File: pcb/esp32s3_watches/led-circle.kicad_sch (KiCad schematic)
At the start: 60 parts

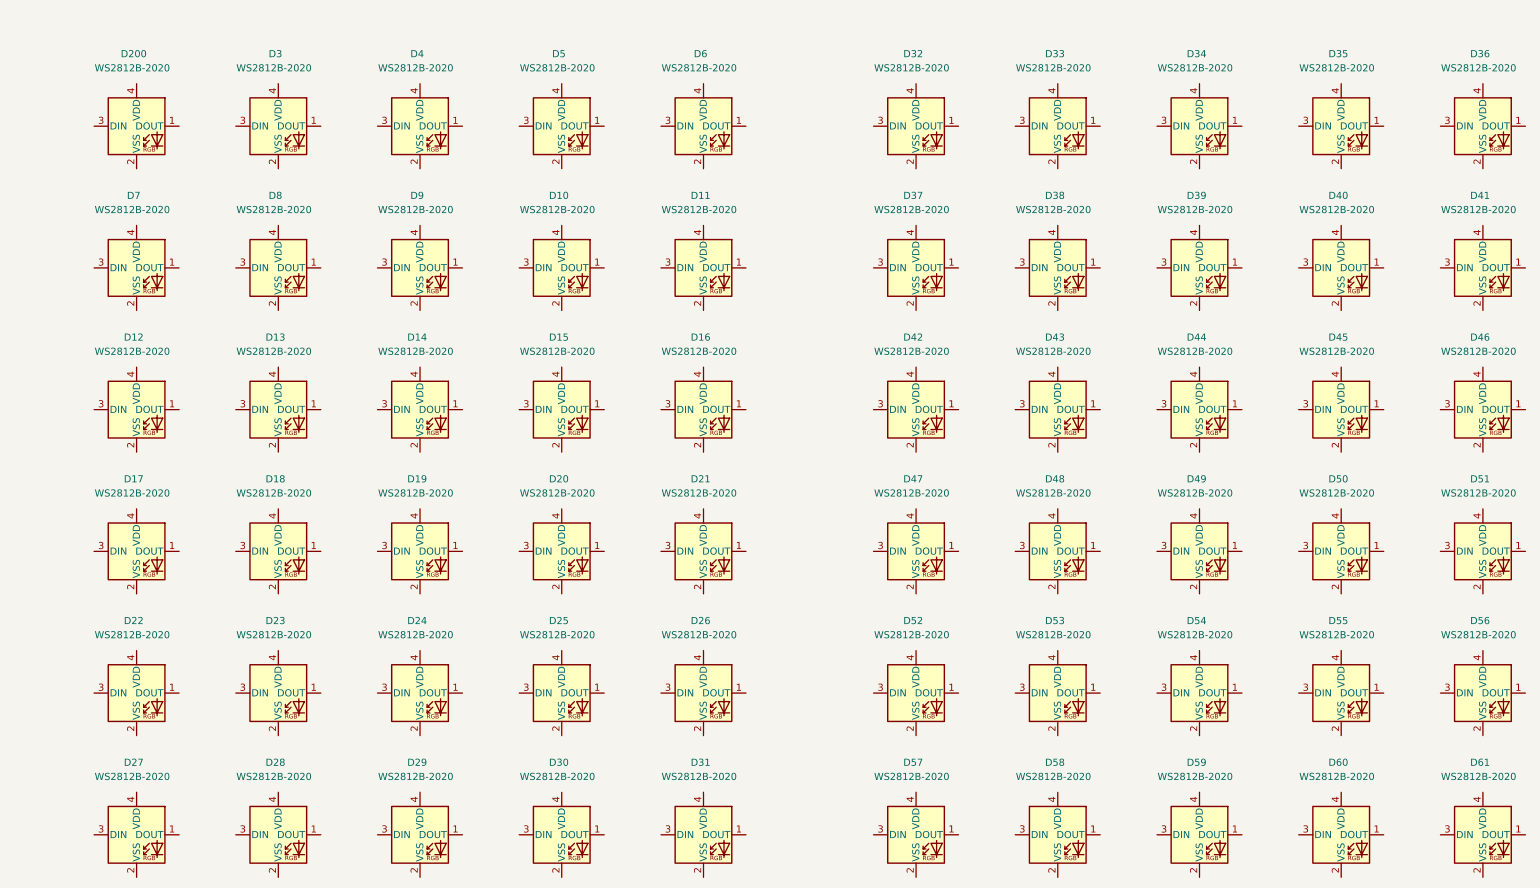
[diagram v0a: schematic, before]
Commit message: Update SD card connection
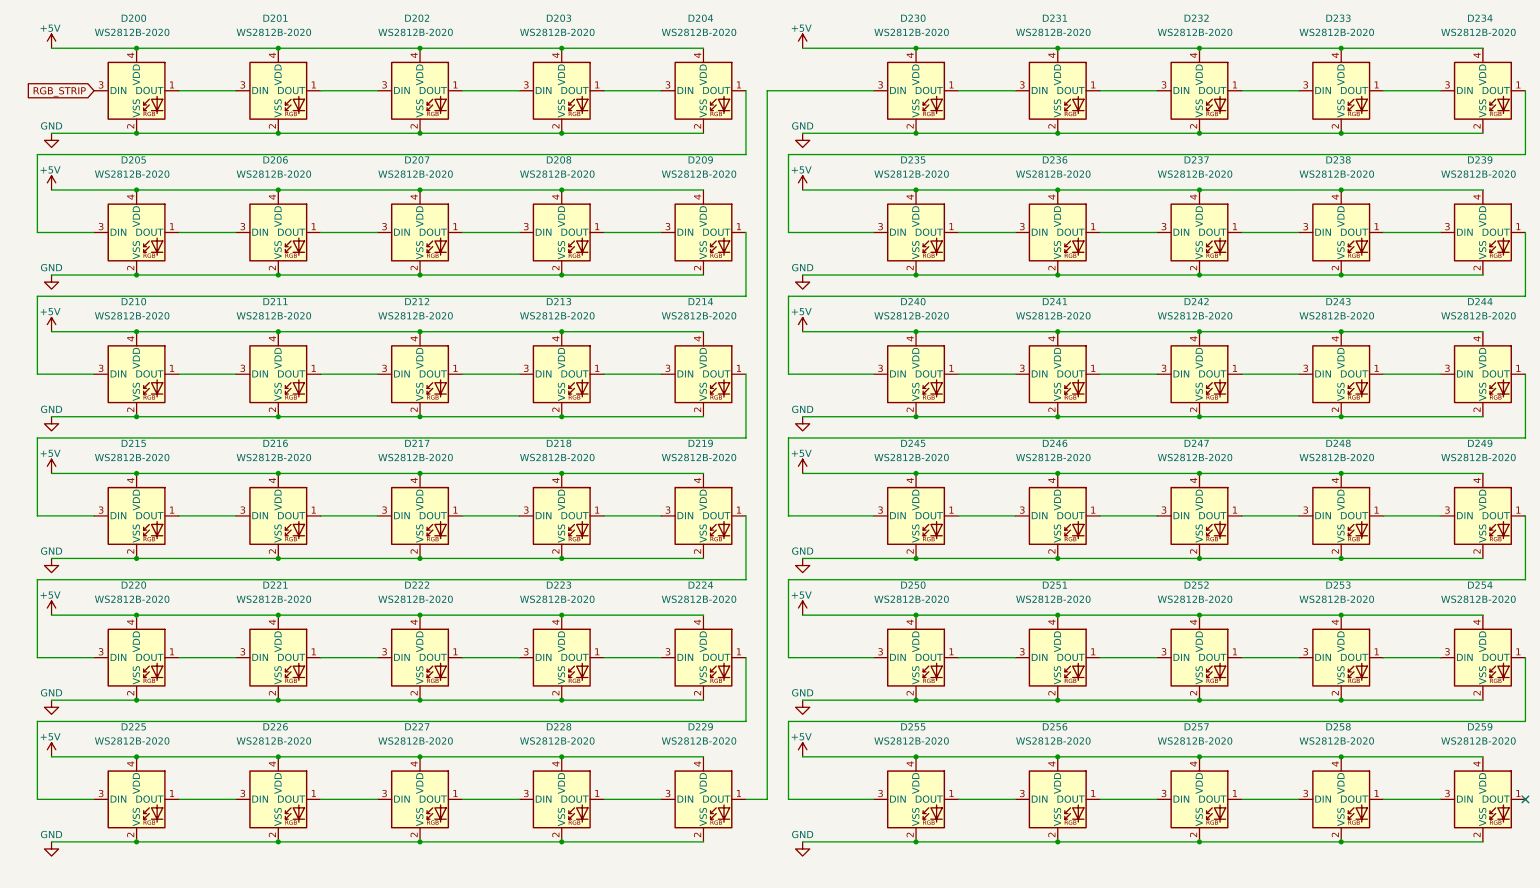
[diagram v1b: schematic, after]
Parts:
- renumbered D3 to D201, D4 to D202, D5 to D203, D6 to D204, D7 to D205, D8 to D206, D9 to D207, D10 to D208, D11 to D209, D12 to D210, D13 to D211, D14 to D212, D15 to D213, D16 to D214, D17 to D215, D18 to D216, D19 to D217, D20 to D218, D21 to D219, D22 to D220, D23 to D221, D24 to D222, D25 to D223, D26 to D224, D27 to D225, D28 to D226, D29 to D227, D30 to D228, D31 to D229, D32 to D230, D33 to D231, D34 to D232, D35 to D233, D36 to D234, D37 to D235, D38 to D236, D39 to D237, D40 to D238, D41 to D239, D42 to D240, D43 to D241, D44 to D242, D45 to D243, D46 to D244, D47 to D245, D48 to D246, D49 to D247, D50 to D248, D51 to D249, D52 to D250, D53 to D251, D54 to D252, D55 to D253, D56 to D254, D57 to D255, D58 to D256, D59 to D257, D60 to D258, D61 to D259
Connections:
- net at D256.1 (DOUT): now also D257.3 (DIN)
- net GND: now reaches D256.2 (VSS)
- net GND: now also D200.2 (VSS), D201.2 (VSS), D202.2 (VSS), D203.2 (VSS), D204.2 (VSS), D205.2 (VSS), D206.2 (VSS), D207.2 (VSS), D208.2 (VSS), D209.2 (VSS), D210.2 (VSS), D211.2 (VSS), D212.2 (VSS), D213.2 (VSS), D214.2 (VSS), D215.2 (VSS), D216.2 (VSS), D217.2 (VSS), D218.2 (VSS), D219.2 (VSS), D220.2 (VSS), D221.2 (VSS), D222.2 (VSS), D223.2 (VSS), D224.2 (VSS), D225.2 (VSS), D226.2 (VSS), D227.2 (VSS), D228.2 (VSS), D229.2 (VSS), D230.2 (VSS), D231.2 (VSS), D232.2 (VSS), D233.2 (VSS), D234.2 (VSS), D235.2 (VSS), D236.2 (VSS), D237.2 (VSS), D238.2 (VSS), D239.2 (VSS), D240.2 (VSS), D241.2 (VSS), D242.2 (VSS), D243.2 (VSS), D244.2 (VSS), D245.2 (VSS), D246.2 (VSS), D247.2 (VSS), D248.2 (VSS), D249.2 (VSS), D250.2 (VSS), D251.2 (VSS), D252.2 (VSS), D253.2 (VSS), D254.2 (VSS), D255.2 (VSS), D257.2 (VSS), D258.2 (VSS), D259.2 (VSS)
- net at D256.3 (DIN): now also D255.1 (DOUT)
- net +5V: now reaches D256.4 (VDD)
- net +5V: now also D200.4 (VDD), D201.4 (VDD), D202.4 (VDD), D203.4 (VDD), D204.4 (VDD), D205.4 (VDD), D206.4 (VDD), D207.4 (VDD), D208.4 (VDD), D209.4 (VDD), D210.4 (VDD), D211.4 (VDD), D212.4 (VDD), D213.4 (VDD), D214.4 (VDD), D215.4 (VDD), D216.4 (VDD), D217.4 (VDD), D218.4 (VDD), D219.4 (VDD), D220.4 (VDD), D221.4 (VDD), D222.4 (VDD), D223.4 (VDD), D224.4 (VDD), D225.4 (VDD), D226.4 (VDD), D227.4 (VDD), D228.4 (VDD), D229.4 (VDD), D230.4 (VDD), D231.4 (VDD), D232.4 (VDD), D233.4 (VDD), D234.4 (VDD), D235.4 (VDD), D236.4 (VDD), D237.4 (VDD), D238.4 (VDD), D239.4 (VDD), D240.4 (VDD), D241.4 (VDD), D242.4 (VDD), D243.4 (VDD), D244.4 (VDD), D245.4 (VDD), D246.4 (VDD), D247.4 (VDD), D248.4 (VDD), D249.4 (VDD), D250.4 (VDD), D251.4 (VDD), D252.4 (VDD), D253.4 (VDD), D254.4 (VDD), D255.4 (VDD), D257.4 (VDD), D258.4 (VDD), D259.4 (VDD)
- net at D246.1 (DOUT): now also D247.3 (DIN)
- net at D246.3 (DIN): now also D245.1 (DOUT)
- net at D215.1 (DOUT): now also D216.3 (DIN)
- net at D215.3 (DIN): now also D214.1 (DOUT)
- net at D200.1 (DOUT): now also D201.3 (DIN)
- net RGB_STRIP: now reaches D200.3 (DIN)
- net at D213.1 (DOUT): now also D214.3 (DIN)
- net at D213.3 (DIN): now also D212.1 (DOUT)
- net at D202.1 (DOUT): now also D203.3 (DIN)
- net at D202.3 (DIN): now also D201.1 (DOUT)
- net at D252.1 (DOUT): now also D253.3 (DIN)
- net at D252.3 (DIN): now also D251.1 (DOUT)
- net at D211.1 (DOUT): now also D212.3 (DIN)
- net at D211.3 (DIN): now also D210.1 (DOUT)
- net at D236.1 (DOUT): now also D237.3 (DIN)
- net at D236.3 (DIN): now also D235.1 (DOUT)
- net at D248.1 (DOUT): now also D249.3 (DIN)
- net at D248.3 (DIN): now also D247.1 (DOUT)
- net at D224.1 (DOUT): now also D225.3 (DIN)
- net at D224.3 (DIN): now also D223.1 (DOUT)
- net at D259.3 (DIN): now also D258.1 (DOUT)
- net at D218.1 (DOUT): now also D219.3 (DIN)
- net at D218.3 (DIN): now also D217.1 (DOUT)
- net at D222.1 (DOUT): now also D223.3 (DIN)
- net at D222.3 (DIN): now also D221.1 (DOUT)
- net at D221.3 (DIN): now also D220.1 (DOUT)
- net at D258.3 (DIN): now also D257.1 (DOUT)
- net at D230.1 (DOUT): now also D231.3 (DIN)
- net at D230.3 (DIN): now also D229.1 (DOUT)
- net at D245.3 (DIN): now also D244.1 (DOUT)
- net at D250.1 (DOUT): now also D251.3 (DIN)
- net at D250.3 (DIN): now also D249.1 (DOUT)
- net at D239.1 (DOUT): now also D240.3 (DIN)
- net at D239.3 (DIN): now also D238.1 (DOUT)
- net at D234.1 (DOUT): now also D235.3 (DIN)
- net at D234.3 (DIN): now also D233.1 (DOUT)
- net at D207.1 (DOUT): now also D208.3 (DIN)
- net at D207.3 (DIN): now also D206.1 (DOUT)
- net at D244.3 (DIN): now also D243.1 (DOUT)
- net at D238.3 (DIN): now also D237.1 (DOUT)
- net at D228.1 (DOUT): now also D229.3 (DIN)
- net at D228.3 (DIN): now also D227.1 (DOUT)
- net at D254.1 (DOUT): now also D255.3 (DIN)
- net at D254.3 (DIN): now also D253.1 (DOUT)
- net at D231.1 (DOUT): now also D232.3 (DIN)
- net at D242.1 (DOUT): now also D243.3 (DIN)
- net at D242.3 (DIN): now also D241.1 (DOUT)
- net at D203.1 (DOUT): now also D204.3 (DIN)
- net at D209.1 (DOUT): now also D210.3 (DIN)
- net at D209.3 (DIN): now also D208.1 (DOUT)
- net at D205.1 (DOUT): now also D206.3 (DIN)
- net at D205.3 (DIN): now also D204.1 (DOUT)
- net at D225.1 (DOUT): now also D226.3 (DIN)
- net at D226.1 (DOUT): now also D227.3 (DIN)
- net at D240.1 (DOUT): now also D241.3 (DIN)
- net at D220.3 (DIN): now also D219.1 (DOUT)
- net at D232.1 (DOUT): now also D233.3 (DIN)
- net at D216.1 (DOUT): now also D217.3 (DIN)
- no-connect marks 0 -> 1
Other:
- moved on the sheet: D200, D201, D202, D203, D204, D205, D206, D207, D208, D209, D210, D211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

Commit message: BOM file updates. Scheme complete.
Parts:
- D200, D201, D202, D203, D204, D205, D206, D207, D208, D209, D210, D211, D212, D213, D214, D215, D216, D217, D218, D219, D220, D221, D222, D223, D224, D225, D226, D227, D228, D229, D230, D231, D232, D233, D234, D235, D236, D237, D238, D239, D240, D241, D242, D243, D244, D245, D246, D247, D248, D249, D250, D251, D252, D253, D254, D255, D256, D257, D258, D259: Manufacturer (none) -> Worldsemi; Manufacturer Product Number (none) -> WS2812B-2020
